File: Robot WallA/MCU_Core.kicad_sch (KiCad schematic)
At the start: 16 parts, among them IC1 STM32F407IGT6, IC2 DS04-254-2-04BK-SMT, J1 Conn_02x05_Female, Y1 Crystal_GND24

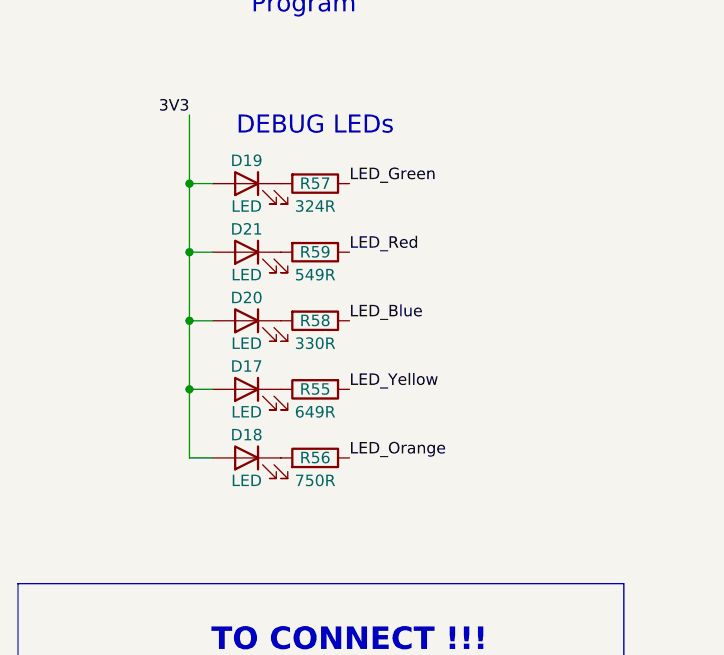
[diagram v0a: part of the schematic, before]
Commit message: Added diode for Type-C connector in case we accidentally power the board with this connector.
Updated fab files
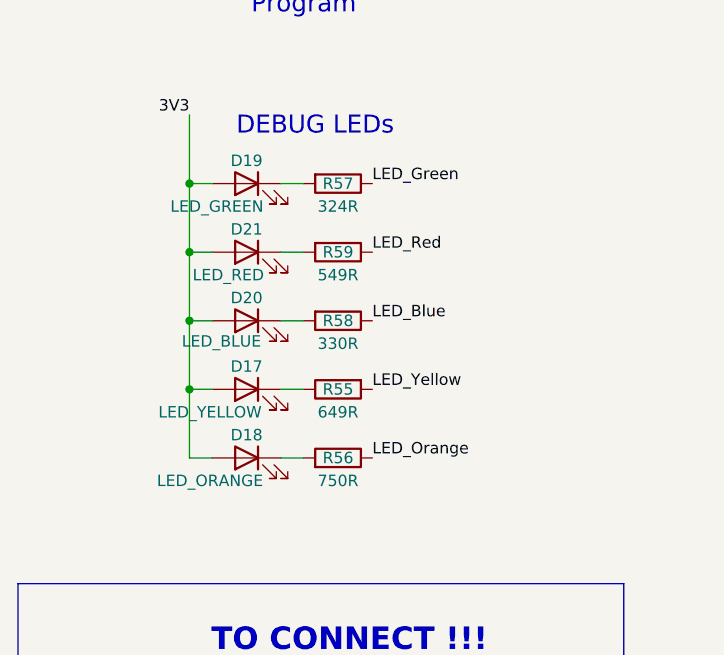
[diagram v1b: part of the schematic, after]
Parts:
- D17: value LED -> LED_YELLOW
- D18: value LED -> LED_ORANGE
- D19: value LED -> LED_GREEN
- D20: value LED -> LED_BLUE
- D21: value LED -> LED_RED
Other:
- moved on the sheet: R55, R56, R57, R58, R59

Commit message: Modified a bit pin header pins to allow I2C,SPI and CAN
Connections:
- net PH13: now reaches IC1.128 (PH13)
- net PI1: now reaches IC1.132 (PI1)
- net PD0: now reaches IC1.142 (PD0)
- net PG14: now reaches IC1.157 (PG14)
- net CurrentSenseMotor1 renamed ADC_PRI_MOTOR_CURRENT_1
- net CurrentSenseMotor2 renamed ADC_PRI_MOTOR_CURRENT_2
- net PD1: no longer names the net of IC1.143 (PD1)
- net PD2: no longer names the net of IC1.144 (PD2)
- net PF8: no longer names the net of IC1.26 (PF8)
- net PG13: no longer names the net of IC1.156 (PG13)
- net SECONDARY_MOTOR0 renamed ADC_SEC_MOTOR_CURRENT_1
- net SECONDARY_MOTOR1 renamed ADC_SEC_MOTOR_CURRENT_2
- net SENSORS0 renamed ADC_SENSOR_1
- net SENSORS1 renamed ADC_SENSOR_2
- net SENSORS2 renamed ADC_SENSOR_3
- net SENSORS3 renamed ADC_SENSOR_4
- net WHEEL6 renamed PRI_MOTOR_NFAULT
- net WHEEL7 renamed PRI_MOTOR_SLEEP
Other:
- note added: "USER INTERFACE"
- note removed: "TO CONNECT !!!"
- moved on the sheet: D17, D18, D19, D20, D21, IC2, R55, R56, R57, R58, R59

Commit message: Added 3 thermistor to measure temperature near 12V and 24V power supplies and near motor drivers
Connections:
- net PF4: now reaches IC1.20 (PF4)
- net ADC_PRI_MOTOR_TEMPERATURE: now reaches IC1.24 (PF6)
- net ADC_POWER_SUPPLIES_TEMPERATURE: now reaches IC1.26 (PF8)
- net PF7 renamed ADC_SEC_MOTOR_TEMPERATURE
- no-connect marks 46 -> 43
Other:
- moved on the sheet: C1, C2, IC1, Y1

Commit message: Modified footprint to simplify BOM. Finalized BOM.
Updated fab files
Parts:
- J1: now left out of the parts list
- R55, R56, R57, R58, R59: footprint Resistor_SMD:R_0603_1608Metric -> Resistor_SMD:R_0603_1608Metric_Pad0.98x0.95mm_HandSolder

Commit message: Corrected schematic labels encoders according to PCB labels... (inversion...)
Add fab files
cleaned
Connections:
- net ENCODER0: now also IC1.101 (PD13); no longer IC1.116 (PC7)
- net ENCODER1: now also IC1.100 (PD12); no longer IC1.115 (PC6)
- net ENCODER2: now also IC1.116 (PC7); no longer IC1.101 (PD13)
- net ENCODER3: now also IC1.115 (PC6); no longer IC1.100 (PD12)
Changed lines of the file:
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@@
 	)
 	(label "ENCODER_RIGHT_2"
-		(at 204.47 53.34 90)
+		(at 166.37 53.34 90)
 		(effects
 			(font
@@
 	)
 	(label "ENCODER_LEFT_2"
-		(at 166.37 53.34 90)
+		(at 204.47 53.34 90)
 		(effects
 			(font
@@
 	)
 	(label "ENCODER_RIGHT_1"
-		(at 201.93 53.34 90)
+		(at 163.83 53.34 90)
 		(effects
 			(font
@@
 	)
 	(label "ENCODER_LEFT_1"
-		(at 163.83 53.34 90)
-		(effects
-			(font
+		(at 201.93 53.34 90)
+		(effects
+			(font
